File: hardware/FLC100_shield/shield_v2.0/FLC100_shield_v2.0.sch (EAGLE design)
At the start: 70 parts, among them IC1 MCP1640, IC2 TSR 1-2450, Q1 2N7000, Q2 2N7000, Q3 2N7000, Q4 2N7000, Q5 2N7000, Q6 2N7000, Q7 2N7000, Q8 2N7000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

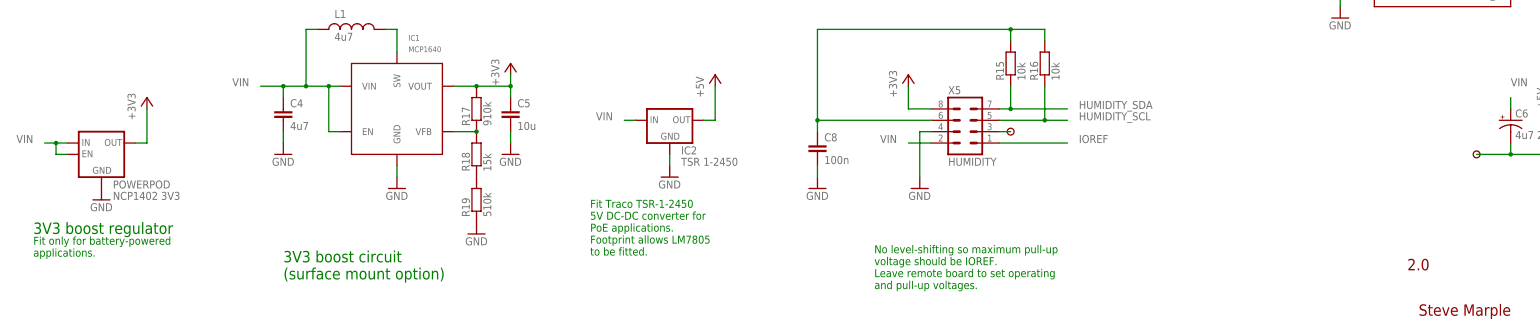
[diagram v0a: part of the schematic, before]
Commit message: Tidied schematic but no circuit changes.
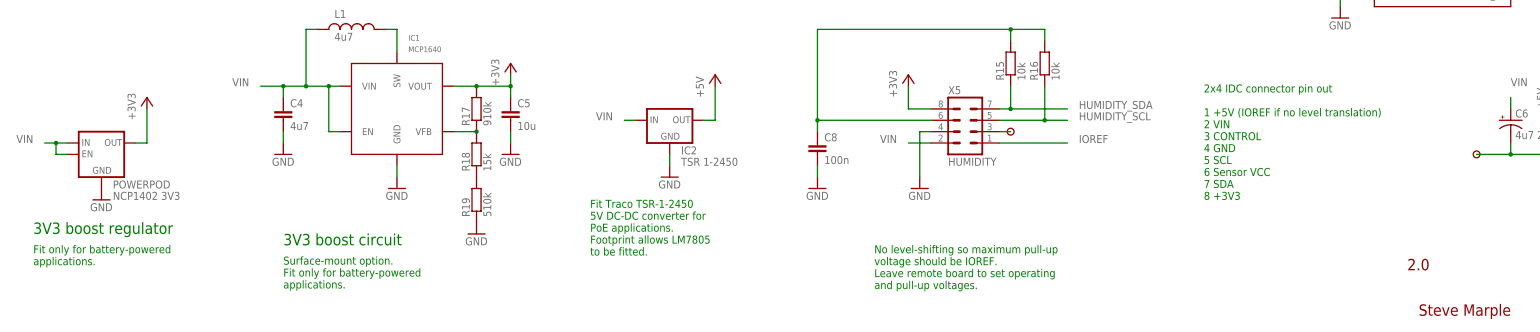
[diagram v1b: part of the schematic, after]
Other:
- note added: "2x4 IDC connector pin out 1 +5V (IOREF if no level translation) 2 VIN 3 CONTROL 4 GND 5 SCL 6 Sensor VCC 7 SDA 8 +3V3"
- note added: "3V3 boost circuit"
- note added: "Surface-mount option. Fit only for battery-powered applications."
- note removed: "3V3 boost circuit (surface mount option)"
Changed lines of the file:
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@@
 <grid distance="0.1" unitdist="inch" unit="inch" style="lines" multiple="1" display="no" altdistance="0.01" altunitdist="inch" altunit="inch"/>
 <layers>
-<layer number="1" name="Top" color="4" fill="1" visible="yes" active="no"/>
-<layer number="2" name="Route2" color="1" fill="3" visible="yes" active="no"/>
-<layer number="3" name="Route3" color="4" fill="3" visible="yes" active="no"/>
-<layer number="14" name="Route14" color="1" fill="6" visible="yes" active="no"/>
-<layer number="15" name="Route15" color="4" fill="6" visible="yes" active="no"/>
-<layer number="16" name="Bottom" color="1" fill="1" visible="yes" active="no"/>
-<layer number="17" name="Pads" color="2" fill="1" visible="yes" active="no"/>
-<layer number="18" name="Vias" color="2" fill="1" visible="yes" active="no"/>
-<layer number="19" name="Unrouted" color="6" fill="1" visible="yes" active="no"/>
-<layer number="20" name="Dimension" color="15" fill="1" visible="yes" active="no"/>
-<layer number="21" name="tPlace" color="7" fill="1" visible="yes" active="no"/>
-<layer number="22" name="bPlace" color="7" fill="1" visible="yes" active="no"/>
-<layer number="23" name="tOrigins" color="15" fill="1" visible="yes" active="no"/>
-<layer number="24" name="bOrigins" color="15" fill="1" visible="yes" active="no"/>
-<layer number="25" name="tNames" color="7" fill="1" visible="yes" active="no"/>
-<layer number="26" name="bNames" color="7" fill="1" visible="yes" active="no"/>
-<layer number="27" name="tValues" color="7" fill="1" visible="yes" active="no"/>
-<layer number="28" name="bValues" color="7" fill="1" visible="yes" active="no"/>
+<layer number="1" name="Top" color="4" fill="1" visible="no" active="no"/>
+<layer number="2" name="Route2" color="1" fill="3" visible="no" active="no"/>
+<layer number="3" name="Route3" color="4" fill="3" visible="no" active="no"/>
+<layer number="14" name="Route14" color="1" fill="6" visible="no" active="no"/>
+<layer number="15" name="Route15" color="4" fill="6" visible="no" active="no"/>
+<layer number="16" name="Bottom" color="1" fill="1" visible="no" active="no"/>
+<layer number="17" name="Pads" color="2" fill="1" visible="no" active="no"/>
+<layer number="18" name="Vias" color="2" fill="1" visible="no" active="no"/>
+<layer number="19" name="Unrouted" color="6" fill="1" visible="no" active="no"/>
+<layer number="20" name="Dimension" color="15" fill="1" visible="no" active="no"/>
+<layer number="21" name="tPlace" color="7" fill="1" visible="no" active="no"/>
+<layer number="22" name="bPlace" color="7" fill="1" visible="no" active="no"/>
+<layer number="23" name="tOrigins" color="15" fill="1" visible="no" active="no"/>
+<layer number="24" name="bOrigins" color="15" fill="1" visible="no" active="no"/>
+<layer number="25" name="tNames" color="7" fill="1" visible="no" active="no"/>
+<layer number="26" name="bNames" color="7" fill="1" visible="no" active="no"/>
+<layer number="27" name="tValues" color="7" fill="1" visible="no" active="no"/>
+<layer number="28" name="bValues" color="7" fill="1" visible="no" active="no"/>
 <layer number="29" name="tStop" color="7" fill="3" visible="no" active="no"/>
 <layer number="30" name="bStop" color="7" fill="6" visible="no" active="no"/>
@@
 <layer number="35" name="tGlue" color="7" fill="4" visible="no" active="no"/>
 <layer number="36" name="bGlue" color="7" fill="5" visible="no" active="no"/>
-<layer number="37" name="tTest" color="7" fill="1" visible="yes" active="no"/>
-<layer number="38" name="bTest" color="7" fill="1" visible="yes" active="no"/>
+<layer number="37" name="tTest" color="7" fill="1" visible="no" active="no"/>
+<layer number="38" name="bTest" color="7" fill="1" visible="no" active="no"/>
 <layer number="39" name="tKeepout" color="4" fill="11" visible="no" active="no"/>
 <layer number="40" name="bKeepout" color="1" fill="11" visible="no" active="no"/>
@@
 <layer number="44" name="Drills" color="7" fill="1" visible="no" active="no"/>
 <layer number="45" name="Holes" color="7" fill="1" visible="no" active="no"/>
-<layer number="46" name="Milling" color="3" fill="1" visible="yes" active="no"/>
-<layer number="47" name="Measures" color="7" fill="1" visible="yes" active="no"/>
-<layer number="48" name="Document" color="7" fill="1" visible="yes" active="no"/>
-<layer number="49" name="Reference" color="7" fill="1" visible="yes" active="no"/>
-<layer number="50" name="dxf" color="7" fill="1" visible="yes" active="no"/>
-<layer number="51" name="tDocu" color="7" fill="1" visible="yes" active="no"/>
-<layer number="52" name="bDocu" color="7" fill="1" visible="yes" active="no"/>
-<layer number="53" name="tGND_GNDA" color="7" fill="9" visible="yes" active="no"/>
-<layer number="54" name="bGND_GNDA" color="1" fill="9" visible="yes" active="no"/>
-<layer number="56" name="wert" color="7" fill="1" visible="yes" active="no"/>
-<layer number="57" name="tCAD" color="7" fill="1" visible="yes" active="no"/>
+<layer number="46" name="Milling" color="3" fill="1" visible="no" active="no"/>
+<layer number="47" name="Measures" color="7" fill="1" visible="no" active="no"/>
+<layer number="48" name="Document" color="7" fill="1" visible="no" active="no"/>
+<layer number="49" name="Reference" color="7" fill="1" visible="no" active="no"/>
+<layer number="50" name="dxf" color="7" fill="1" visible="no" active="no"/>
+<layer number="51" name="tDocu" color="7" fill="1" visible="no" active="no"/>
+<layer number="52" name="bDocu" color="7" fill="1" visible="no" active="no"/>
+<layer number="53" name="tGND_GNDA" color="7" fill="9" visible="no" active="no"/>
+<layer number="54" name="bGND_GNDA" color="1" fill="9" visible="no" active="no"/>
+<layer number="56" name="wert" color="7" fill="1" visible="no" active="no"/>
+<layer number="57" name="tCAD" color="7" fill="1" visible="no" active="no"/>
 <layer number="91" name="Nets" color="2" fill="1" visible="yes" active="yes"/>
 <layer number="92" name="Busses" color="1" fill="1" visible="yes" active="yes"/>
@@
 <text x="327.66" y="139.7" size="2.54" layer="91">Temperature sensor</text>
 <text x="20.32" y="22.86" size="2.54" layer="91">3V3 boost regulator</text>
-<text x="20.32" y="17.78" size="1.778" layer="91">Fit only for battery-powered
+<text x="20.32" y="20.32" size="1.778" layer="91" align="top-left">Fit only for battery-powered
 applications.</text>
 <text x="144.78" y="30.48" size="1.778" layer="91" align="top-left">Fit Traco TSR-1-2450
@@
 Footprint allows LM7805
 to be fitted.</text>
-<text x="76.2" y="12.7" size="2.54" layer="91">3V3 boost circuit
-(surface mount option)</text>
+<text x="76.2" y="20.32" size="2.54" layer="91">3V3 boost circuit</text>
 <wire x1="45.72" y1="185.42" x2="50.8" y2="180.34" width="0.1524" layer="94" style="shortdash"/>
 <wire x1="50.8" y1="180.34" x2="91.44" y2="180.34" width="0.1524" layer="94" style="shortdash"/>
@@
 May omit one diode and replace other by
 wire link when voltages known in advance.</text>
+<text x="281.94" y="30.48" size="1.778" layer="91">2x4 IDC connector pin out
+1 +5V (IOREF if no level translation)
+2 VIN
+3 CONTROL
+4 GND
+5 SCL
+6 Sensor VCC
+7 SDA
+8 +3V3</text>
+<text x="76.2" y="17.78" size="1.778" layer="91" align="top-left">Surface-mount option.
+Fit only for battery-powered
+applications.</text>
 </plain>
 <instances>

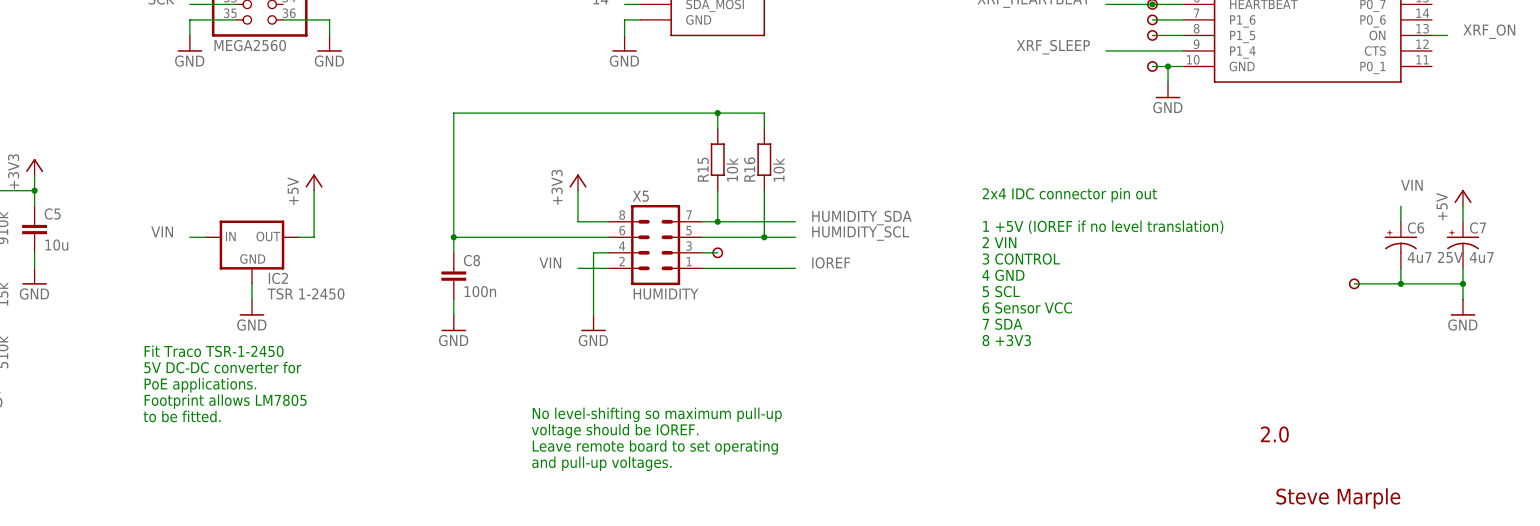
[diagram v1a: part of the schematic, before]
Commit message: Adding extra decoupling for 3.3V.
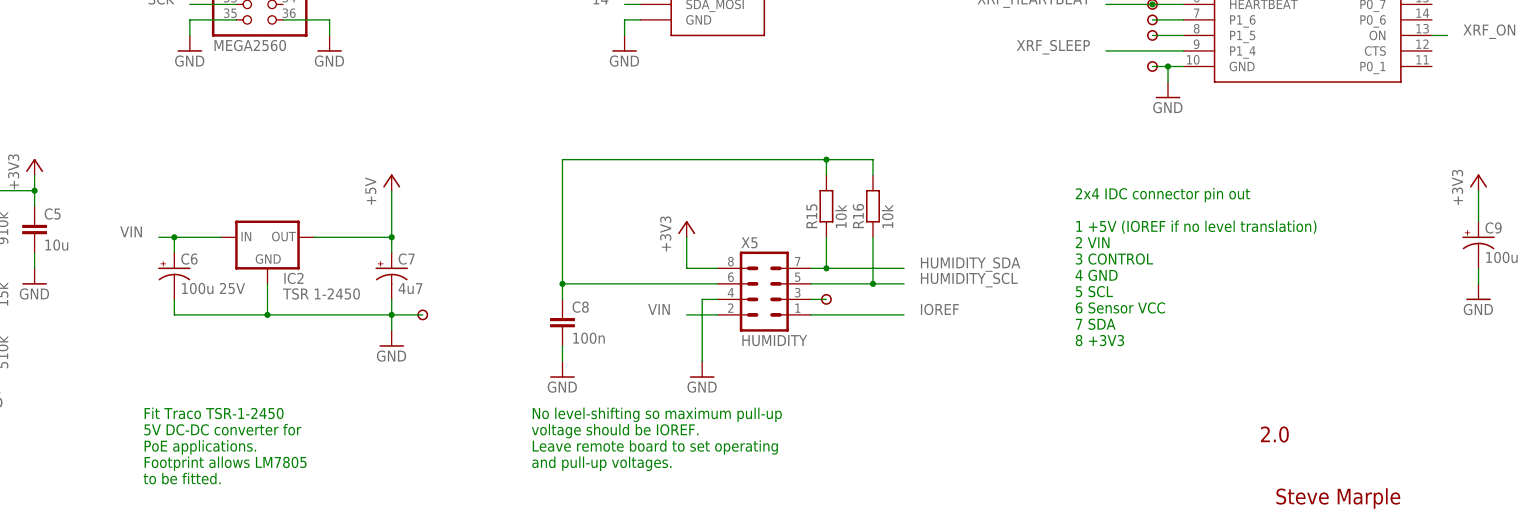
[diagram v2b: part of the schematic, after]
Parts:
- added C9: 100u, SteveMarple:CAP_POLPTH2
- C6: value 4u7 25V -> 100u 25V
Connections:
- net +3V3: now also C9.+
- net GND: now also C9.-
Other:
- moved on the sheet: C6, C7, C8, IC2, R15, R16, X5

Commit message: Fixing silkscreen and generating Gerber files.
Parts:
- renumbered MOD-1 to MOD1
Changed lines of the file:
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@@
 <grid distance="0.1" unitdist="inch" unit="inch" style="lines" multiple="1" display="no" altdistance="0.01" altunitdist="inch" altunit="inch"/>
 <layers>
-<layer number="1" name="Top" color="4" fill="1" visible="no" active="no"/>
-<layer number="2" name="Route2" color="1" fill="3" visible="no" active="no"/>
-<layer number="3" name="Route3" color="4" fill="3" visible="no" active="no"/>
-<layer number="14" name="Route14" color="1" fill="6" visible="no" active="no"/>
-<layer number="15" name="Route15" color="4" fill="6" visible="no" active="no"/>
-<layer number="16" name="Bottom" color="1" fill="1" visible="no" active="no"/>
-<layer number="17" name="Pads" color="2" fill="1" visible="no" active="no"/>
-<layer number="18" name="Vias" color="2" fill="1" visible="no" active="no"/>
-<layer number="19" name="Unrouted" color="6" fill="1" visible="no" active="no"/>
-<layer number="20" name="Dimension" color="15" fill="1" visible="no" active="no"/>
-<layer number="21" name="tPlace" color="7" fill="1" visible="no" active="no"/>
-<layer number="22" name="bPlace" color="7" fill="1" visible="no" active="no"/>
-<layer number="23" name="tOrigins" color="15" fill="1" visible="no" active="no"/>
-<layer number="24" name="bOrigins" color="15" fill="1" visible="no" active="no"/>
-<layer number="25" name="tNames" color="7" fill="1" visible="no" active="no"/>
-<layer number="26" name="bNames" color="7" fill="1" visible="no" active="no"/>
-<layer number="27" name="tValues" color="7" fill="1" visible="no" active="no"/>
-<layer number="28" name="bValues" color="7" fill="1" visible="no" active="no"/>
+<layer number="1" name="Top" color="4" fill="1" visible="yes" active="no"/>
+<layer number="2" name="Route2" color="1" fill="3" visible="yes" active="no"/>
+<layer number="3" name="Route3" color="4" fill="3" visible="yes" active="no"/>
+<layer number="14" name="Route14" color="1" fill="6" visible="yes" active="no"/>
+<layer number="15" name="Route15" color="4" fill="6" visible="yes" active="no"/>
+<layer number="16" name="Bottom" color="1" fill="1" visible="yes" active="no"/>
+<layer number="17" name="Pads" color="2" fill="1" visible="yes" active="no"/>
+<layer number="18" name="Vias" color="2" fill="1" visible="yes" active="no"/>
+<layer number="19" name="Unrouted" color="6" fill="1" visible="yes" active="no"/>
+<layer number="20" name="Dimension" color="15" fill="1" visible="yes" active="no"/>
+<layer number="21" name="tPlace" color="7" fill="1" visible="yes" active="no"/>
+<layer number="22" name="bPlace" color="7" fill="1" visible="yes" active="no"/>
+<layer number="23" name="tOrigins" color="15" fill="1" visible="yes" active="no"/>
+<layer number="24" name="bOrigins" color="15" fill="1" visible="yes" active="no"/>
+<layer number="25" name="tNames" color="7" fill="1" visible="yes" active="no"/>
+<layer number="26" name="bNames" color="7" fill="1" visible="yes" active="no"/>
+<layer number="27" name="tValues" color="7" fill="1" visible="yes" active="no"/>
+<layer number="28" name="bValues" color="7" fill="1" visible="yes" active="no"/>
 <layer number="29" name="tStop" color="7" fill="3" visible="no" active="no"/>
 <layer number="30" name="bStop" color="7" fill="6" visible="no" active="no"/>
@@
 <layer number="35" name="tGlue" color="7" fill="4" visible="no" active="no"/>
 <layer number="36" name="bGlue" color="7" fill="5" visible="no" active="no"/>
-<layer number="37" name="tTest" color="7" fill="1" visible="no" active="no"/>
-<layer number="38" name="bTest" color="7" fill="1" visible="no" active="no"/>
+<layer number="37" name="tTest" color="7" fill="1" visible="yes" active="no"/>
+<layer number="38" name="bTest" color="7" fill="1" visible="yes" active="no"/>
 <layer number="39" name="tKeepout" color="4" fill="11" visible="no" active="no"/>
 <layer number="40" name="bKeepout" color="1" fill="11" visible="no" active="no"/>
@@
 <layer number="44" name="Drills" color="7" fill="1" visible="no" active="no"/>
 <layer number="45" name="Holes" color="7" fill="1" visible="no" active="no"/>
-<layer number="46" name="Milling" color="3" fill="1" visible="no" active="no"/>
-<layer number="47" name="Measures" color="7" fill="1" visible="no" active="no"/>
-<layer number="48" name="Document" color="7" fill="1" visible="no" active="no"/>
-<layer number="49" name="Reference" color="7" fill="1" visible="no" active="no"/>
-<layer number="50" name="dxf" color="7" fill="1" visible="no" active="no"/>
-<layer number="51" name="tDocu" color="7" fill="1" visible="no" active="no"/>
-<layer number="52" name="bDocu" color="7" fill="1" visible="no" active="no"/>
-<layer number="53" name="tGND_GNDA" color="7" fill="9" visible="no" active="no"/>
-<layer number="54" name="bGND_GNDA" color="1" fill="9" visible="no" active="no"/>
-<layer number="56" name="wert" color="7" fill="1" visible="no" active="no"/>
-<layer number="57" name="tCAD" color="7" fill="1" visible="no" active="no"/>
+<layer number="46" name="Milling" color="3" fill="1" visible="yes" active="no"/>
+<layer number="47" name="Measures" color="7" fill="1" visible="yes" active="no"/>
+<layer number="48" name="Document" color="7" fill="1" visible="yes" active="no"/>
+<layer number="49" name="Reference" color="7" fill="1" visible="yes" active="no"/>
+<layer number="50" name="dxf" color="7" fill="1" visible="yes" active="no"/>
+<layer number="51" name="tDocu" color="7" fill="1" visible="yes" active="no"/>
+<layer number="52" name="bDocu" color="7" fill="1" visible="yes" active="no"/>
+<layer number="53" name="tGND_GNDA" color="7" fill="9" visible="yes" active="no"/>
+<layer number="54" name="bGND_GNDA" color="1" fill="9" visible="yes" active="no"/>
+<layer number="56" name="wert" color="7" fill="1" visible="yes" active="no"/>
+<layer number="57" name="tCAD" color="7" fill="1" visible="yes" active="no"/>
 <layer number="91" name="Nets" color="2" fill="1" visible="yes" active="yes"/>
 <layer number="92" name="Busses" color="1" fill="1" visible="yes" active="yes"/>
@@
 <part name="GND2" library="supply1" deviceset="GND" device=""/>
 <part name="X2" library="SteveMarple" deviceset="RJ11-6" device="PTH" value="RJ11"/>
-<part name="MOD-1" library="SteveMarple" deviceset="EMBEDDED_ADVENTURES_MOD-1016" device="NO-HOLES" value=""/>
+<part name="MOD1" library="SteveMarple" deviceset="EMBEDDED_ADVENTURES_MOD-1016" device="NO-HOLES" value=""/>
 <part name="GND3" library="supply1" deviceset="GND" device=""/>
 <part name="X5" library="SteveMarple" deviceset="ML8" device="" value="HUMIDITY"/>
@@
 <instance part="GND2" gate="1" x="175.26" y="78.74"/>
 <instance part="X2" gate="G$1" x="304.8" y="182.88" rot="R180"/>
-<instance part="MOD-1" gate="G$1" x="238.76" y="91.44"/>
+<instance part="MOD1" gate="G$1" x="238.76" y="91.44"/>
 <instance part="GND3" gate="1" x="223.52" y="78.74"/>
 <instance part="X5" gate="G$1" x="246.38" y="38.1"/>
@@
 </segment>
 <segment>
-<pinref part="MOD-1" gate="G$1" pin="GND"/>
+<pinref part="MOD1" gate="G$1" pin="GND"/>
 <pinref part="GND3" gate="1" pin="GND"/>
 <wire x1="226.06" y1="83.82" x2="223.52" y2="83.82" width="0.1524" layer="91"/>
@@
 </segment>
 <segment>
-<pinref part="MOD-1" gate="G$1" pin="VCC"/>
+<pinref part="MOD1" gate="G$1" pin="VCC"/>
 <wire x1="226.06" y1="99.06" x2="223.52" y2="99.06" width="0.1524" layer="91"/>
 <wire x1="223.52" y1="99.06" x2="223.52" y2="104.14" width="0.1524" layer="91"/>
@@
 </segment>
 <segment>
-<pinref part="MOD-1" gate="G$1" pin="IRQ"/>
+<pinref part="MOD1" gate="G$1" pin="IRQ"/>
 <wire x1="226.06" y1="93.98" x2="223.52" y2="93.98" width="0.1524" layer="91"/>
 <label x="220.98" y="93.98" size="1.778" layer="95" rot="MR0"/>
@@
 </segment>
 <segment>
-<pinref part="MOD-1" gate="G$1" pin="SDA_MOSI"/>
+<pinref part="MOD1" gate="G$1" pin="SDA_MOSI"/>
 <wire x1="226.06" y1="86.36" x2="223.52" y2="86.36" width="0.1524" layer="91"/>
 <label x="220.98" y="86.36" size="1.778" layer="95" rot="MR0"/>
@@
 </segment>
 <segment>
-<pinref part="MOD-1" gate="G$1" pin="SCL"/>
+<pinref part="MOD1" gate="G$1" pin="SCL"/>
 <wire x1="226.06" y1="91.44" x2="223.52" y2="91.44" width="0.1524" layer="91"/>
 <label x="220.98" y="91.44" size="1.778" layer="95" rot="MR0"/>
